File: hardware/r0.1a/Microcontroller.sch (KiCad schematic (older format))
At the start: 71 parts, among them J1 STLink, J2 USB_C, J3 OLED, SW1 Button 1, SW2 Button 2, SW3 Reset, SW4 Rotary, U1 USBLC6-2, U2 W25Q16, U3 STM32F407VETx, U4 LM1117-3.3, Y1 8 MHz

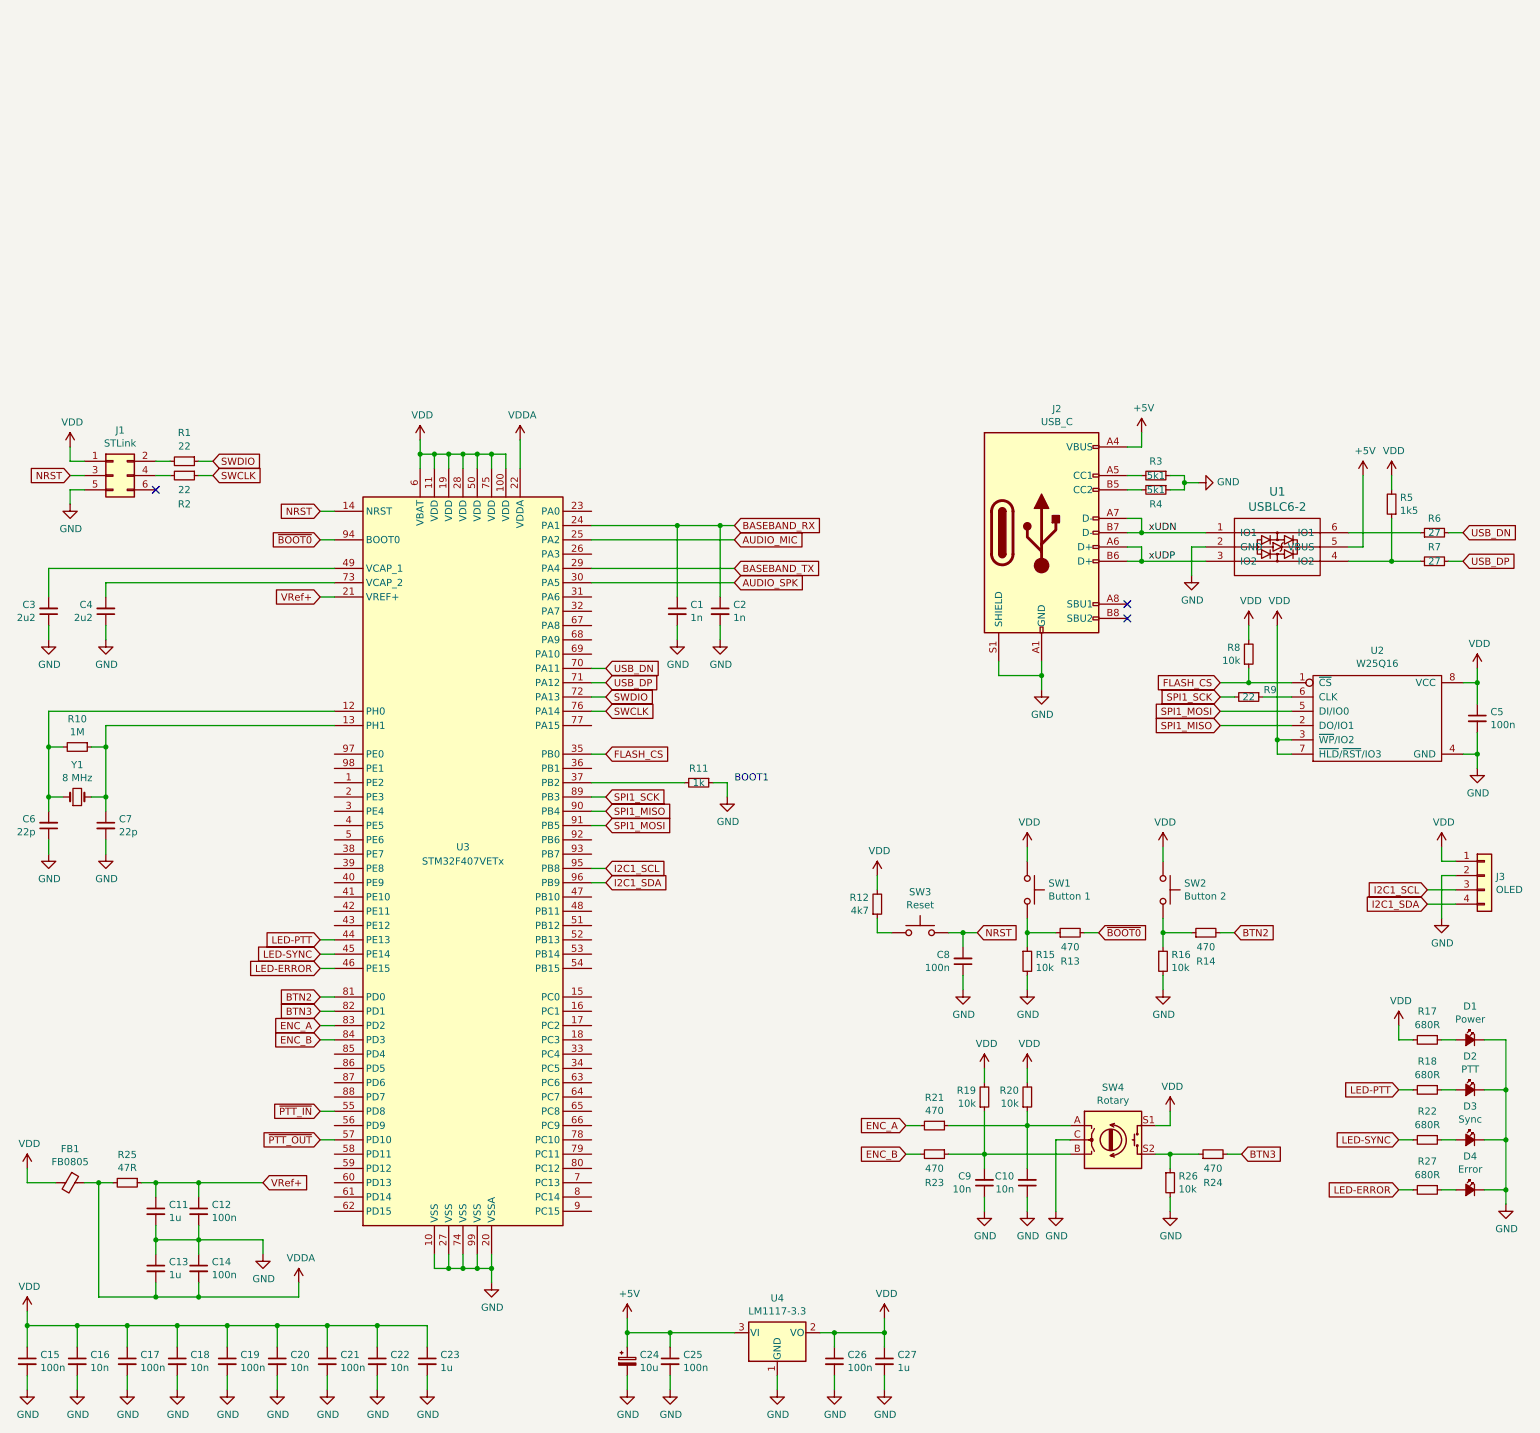
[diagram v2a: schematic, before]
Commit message: Small fixes / updates
* Fixed library path
* Added 12 MHz TCXO
* Replaced rotary encoder with more buttons
* Changed radio connector pinout to be compatible with Repeater Builder and BI7JTA modem boards
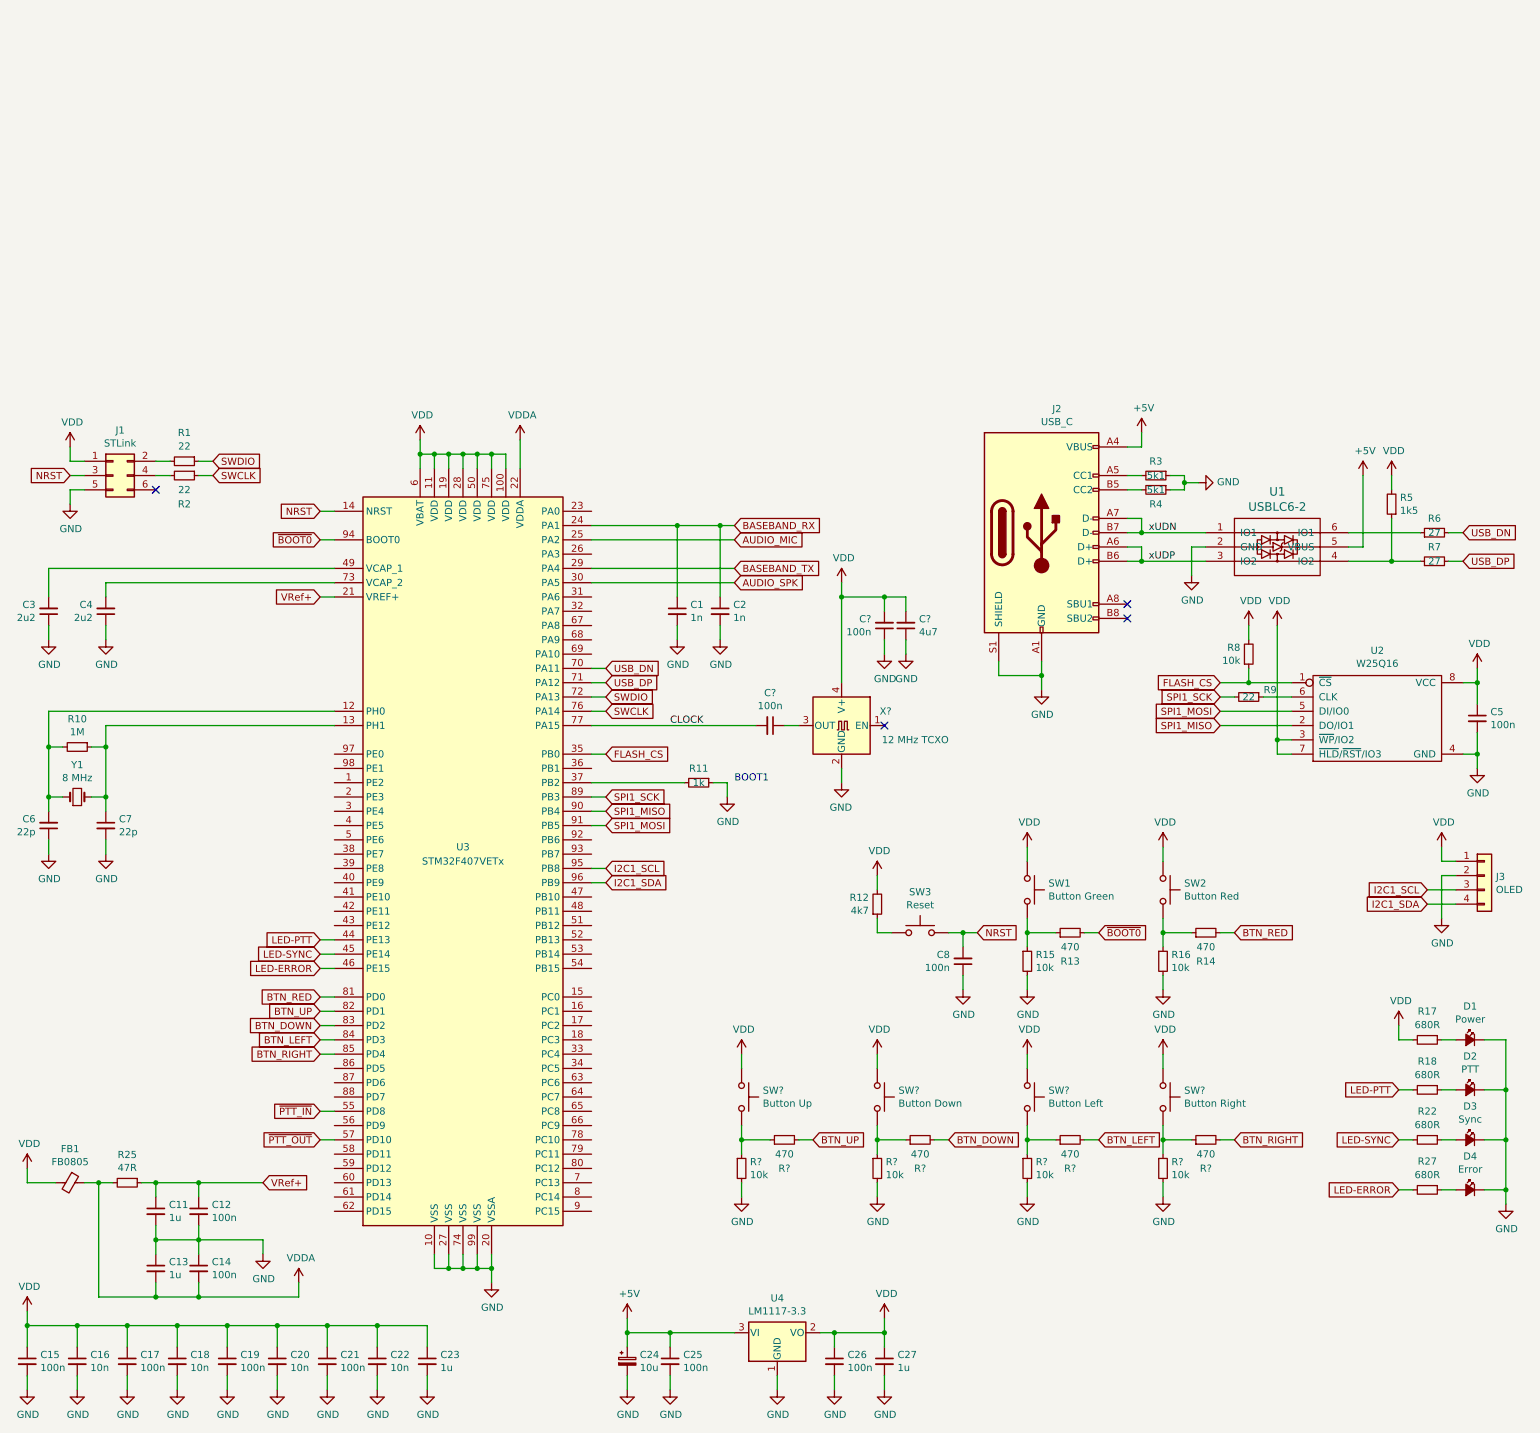
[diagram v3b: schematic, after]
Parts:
- removed C10, C9: 10n, symbol pkl_device:pkl_C_Small
- removed R19, R20, R26: 10k, symbol pkl_device:pkl_R_Small
- removed R21, R23, R24: 470, symbol pkl_device:pkl_R_Small
- removed SW4: Rotary, symbol Device:Rotary_Encoder_Switch
- added C? (x2): 100n, symbol pkl_device:pkl_C_Small
- added C?: 4u7, symbol pkl_device:pkl_C_Small
- added R? (x4): 10k, symbol pkl_device:pkl_R_Small
- added R? (x4): 470, symbol pkl_device:pkl_R_Small
- added SW?: Button Up, symbol Switch:SW_Push
- added SW?: Button Down, symbol Switch:SW_Push
- added SW?: Button Left, symbol Switch:SW_Push
- added SW?: Button Right, symbol Switch:SW_Push
- added X?: 12 MHz TCXO, Oscillator:Oscillator_SMD_EuroQuartz_XO32-4Pin_3.2x2.5mm, symbol Oscillator:XO32
- SW1: value Button 1 -> Button Green
- SW2: value Button 2 -> Button Red
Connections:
- net GND: now also C?.1, C?.1, R?.2, R?.2, R?.2, R?.2, X?.2 (GND)
- net VDD: now also C?.2, C?.2, SW?.1, SW?.1, SW?.1, SW?.1, X?.4 (V+)
- net CLOCK: now reaches U3.77 (PA15)
- net CLOCK: now also C?.2
- net BTN_RIGHT: now reaches U3.85 (PD4)
- net BTN_RIGHT: now also R?.2
- net BTN2 renamed BTN_RED
- net BTN3 renamed BTN_UP
- net BTN_UP: now also R?.2
- net ENC_A renamed BTN_DOWN
- net BTN_DOWN: now also R?.2
- net ENC_B renamed BTN_LEFT
- net BTN_LEFT: now also R?.2
- new net: C?.1, X?.3 (OUT)
- new net: R?.1, R?.1, SW?.2 (x4)
- no-connect marks 3 -> 4

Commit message: Replaced Xtal parallel R with series R
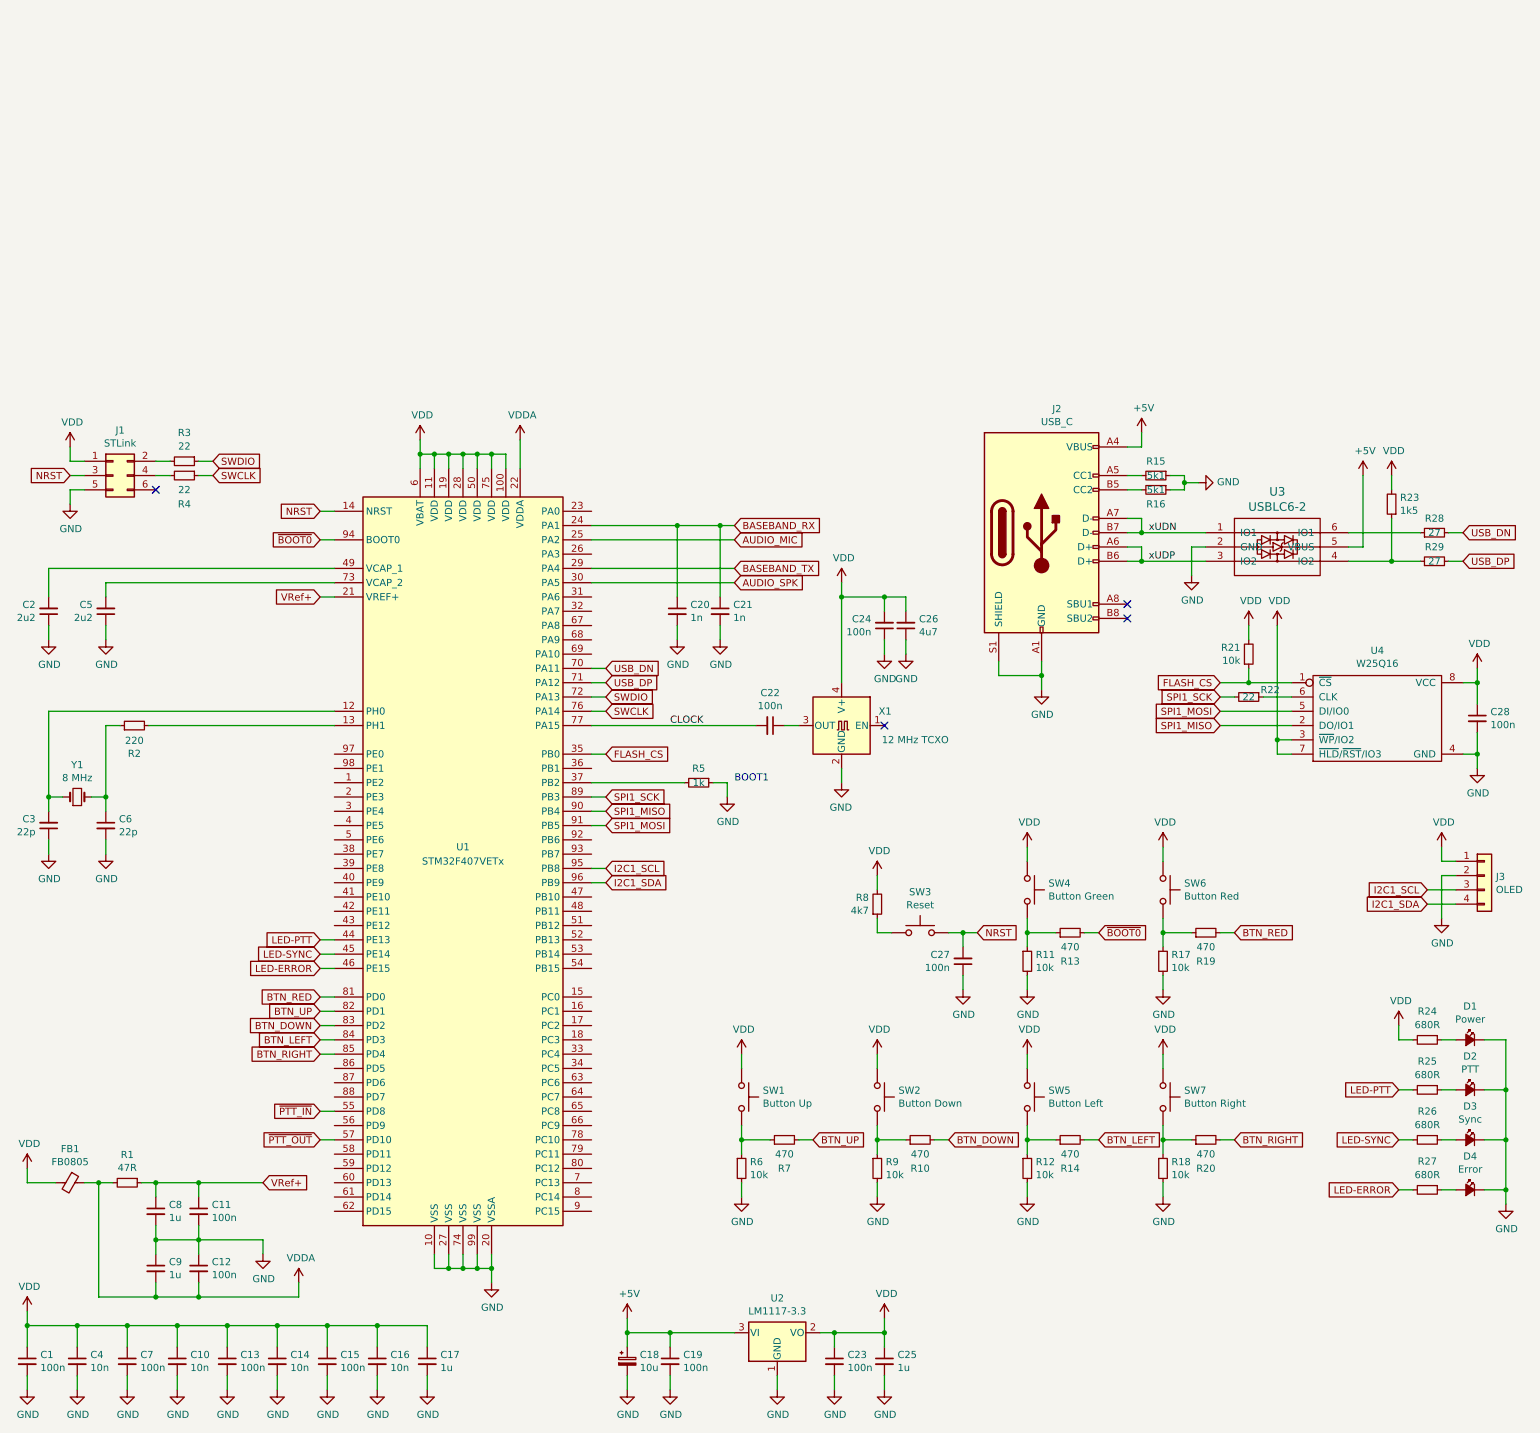
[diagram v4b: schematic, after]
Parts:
- R2: renamed from R10; value 1M -> 220
- gave numbers to parts that had none: 16
- renumbered C15 to C1, C18 to C10, C12 to C11, C14 to C12, C19 to C13, C20 to C14, C21 to C15, C22 to C16, C23 to C17, C24 to C18, C25 to C19, C3 to C2, C1 to C20, C2 to C21, C26 to C23, C27 to C25, C8 to C27, C5 to C28, C6 to C3, C16 to C4, C4 to C5, C7 to C6, C17 to C7, C11 to C8, C13 to C9, R25 to R1, R15 to R11, R3 to R15, R4 to R16, R16 to R17, R14 to R19, R8 to R21, R9 to R22, R5 to R23, R17 to R24, R18 to R25, R22 to R26, R6 to R28, R7 to R29, R1 to R3, R2 to R4, R11 to R5, R12 to R8, SW1 to SW4, SW2 to SW6, U3 to U1, U4 to U2, U1 to U3, U2 to U4
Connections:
- net at C3.2, U1.12 (PH0), Y1.1: no longer R2.2
- net at C6.1, R2.1, Y1.2: no longer U1.13 (PH1)
- new net: R2.2, U1.13 (PH1)
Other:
- moved on the sheet: R2
